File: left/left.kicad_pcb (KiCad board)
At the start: 2 copper layers, 117.6 x 97.9 mm, 53 parts, among them J1 USB_C_Receptacle_IN, J2 USB_C_Receptacle_OUT, SW1 SW_Push, SW2 SW_SPDT, U1 STM32G0B1CBTx, U2 SRV05-4, U3 XC6206P332MR, U4 SRV05-4

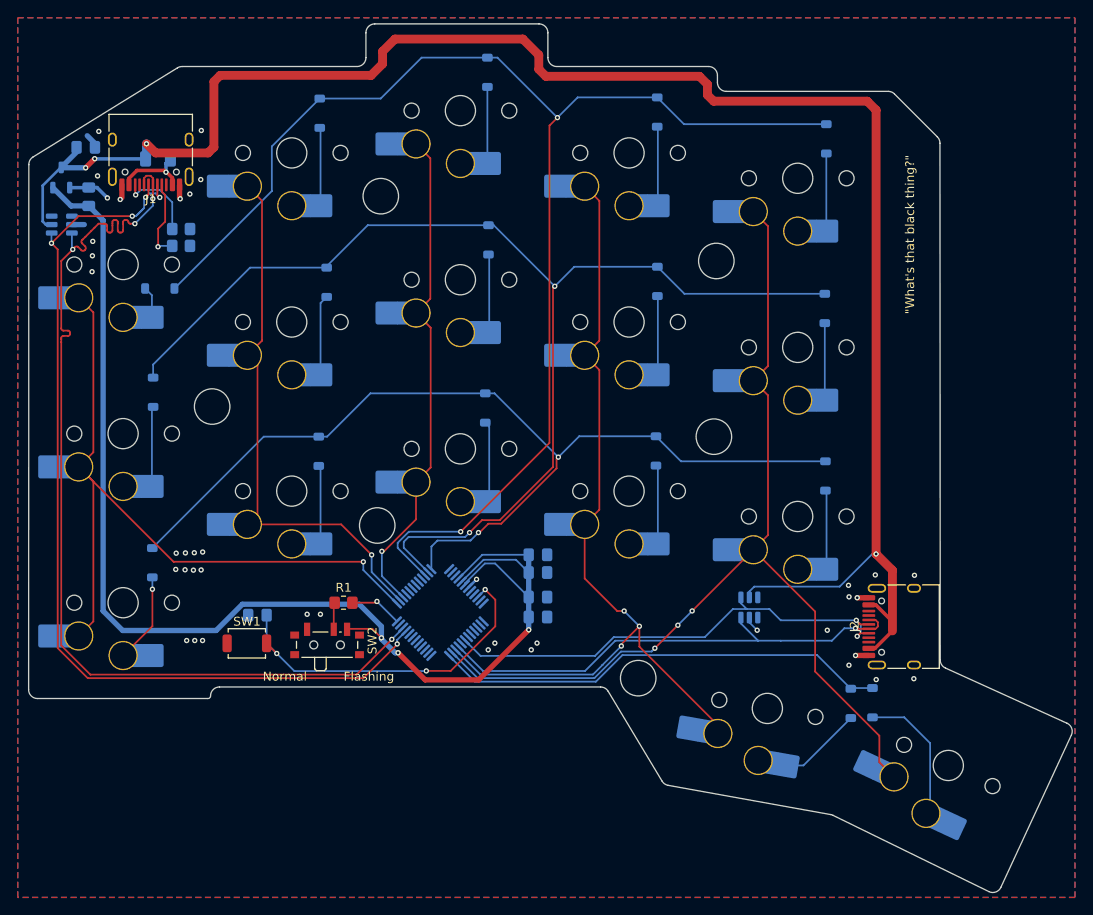
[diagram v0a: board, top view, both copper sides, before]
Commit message: needed to move the usbs on left side
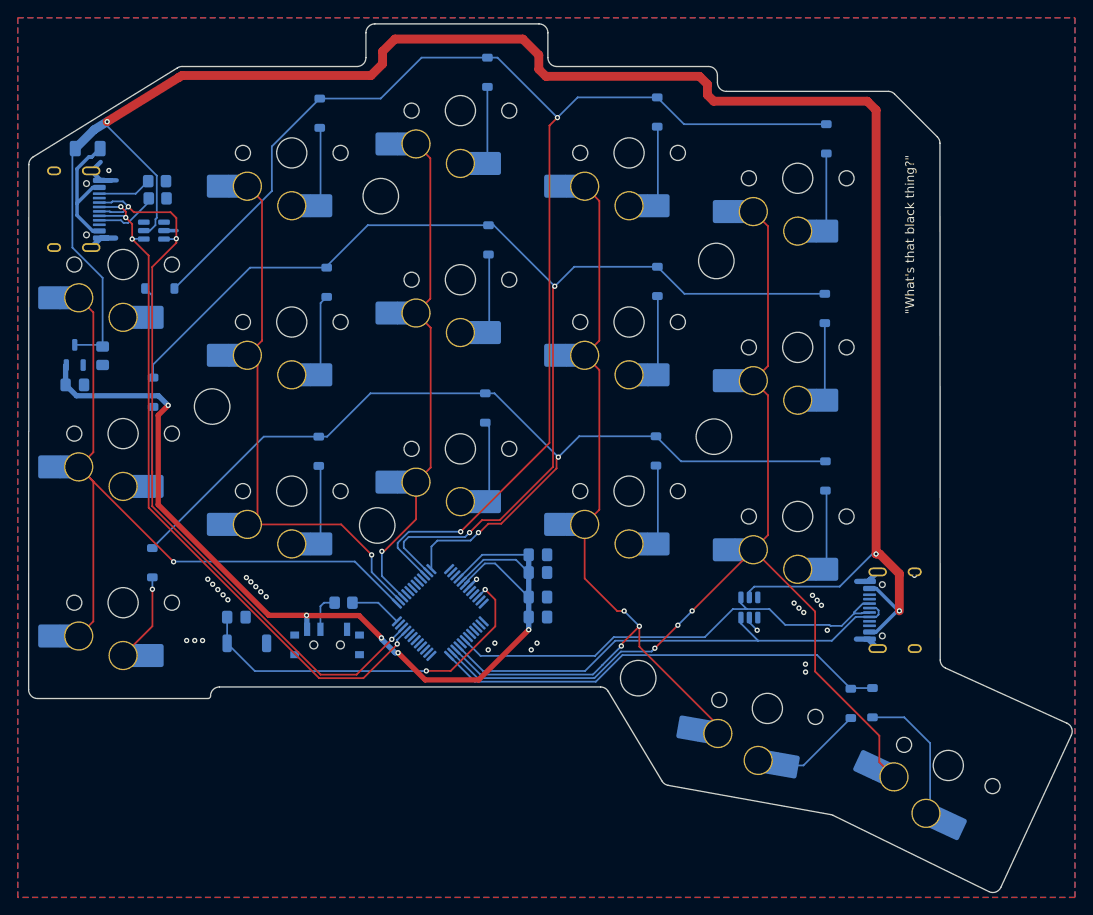
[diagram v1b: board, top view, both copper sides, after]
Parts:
- J1, J2, R1, SW1, SW2: moved to B.Cu
- moved C6 23.6 mm to (54.9, 83.4), turned to -90 degrees
- moved C7 21.3 mm to (51.7, 86.7), turned to 0 degrees
- moved U3 20.0 mm to (51.7, 83.3)
- moved J1 12.0 mm to (50.4, 66.9), turned to 90 degrees
- moved U4 10.4 mm to (60.6, 69.3)
- moved F1 8.00 mm to (53.2, 60.0)
- moved R2 6.03 mm to (61.0, 63.7)
- moved R3 5.97 mm to (61.1, 65.7)
- moved C5 2.38 mm to (69.9, 112.8), turned to 0 degrees
- moved J2 1.84 mm to (145.3, 112.0), turned to -90 degrees
- turned SW1 to 0 degrees
- turned SW2 to 180 degrees
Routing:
- net +3.3V: track 148.8 -> 116.8 mm, vias 3 -> 5
- net D-: track 109.7 -> 80.7 mm, vias 5 -> 4
- net D+: track 113.0 -> 85.8 mm, vias 4 -> 3
- net +5V: track 205.4 -> 226.2 mm, vias 4 -> 3
- net VBUS: track 8.91 -> 16.1 mm, vias 1 -> 0
- net Net-(J1-CC2): track 9.56 -> 5.66 mm, vias 1 -> 0
- net GND: track 17.4 -> 20.1 mm, vias 40 -> 30
- net nRST: track 40.0 -> 42.5 mm, vias 3 -> 2
- net Net-(J1-CC1): track 9.11 -> 6.65 mm, vias 1 -> 0
- net Net-(SW2-B): track 3.04 -> 4.36 mm
- net RX: track 54.6 -> 53.8 mm, vias 2 -> 0
- net COL4: track 83.6 -> 83.1 mm
- net TX: track 55.6 -> 56.1 mm, vias 1 -> 0
- net BOOT0: track 6.00 -> 5.88 mm, vias 1 -> 0

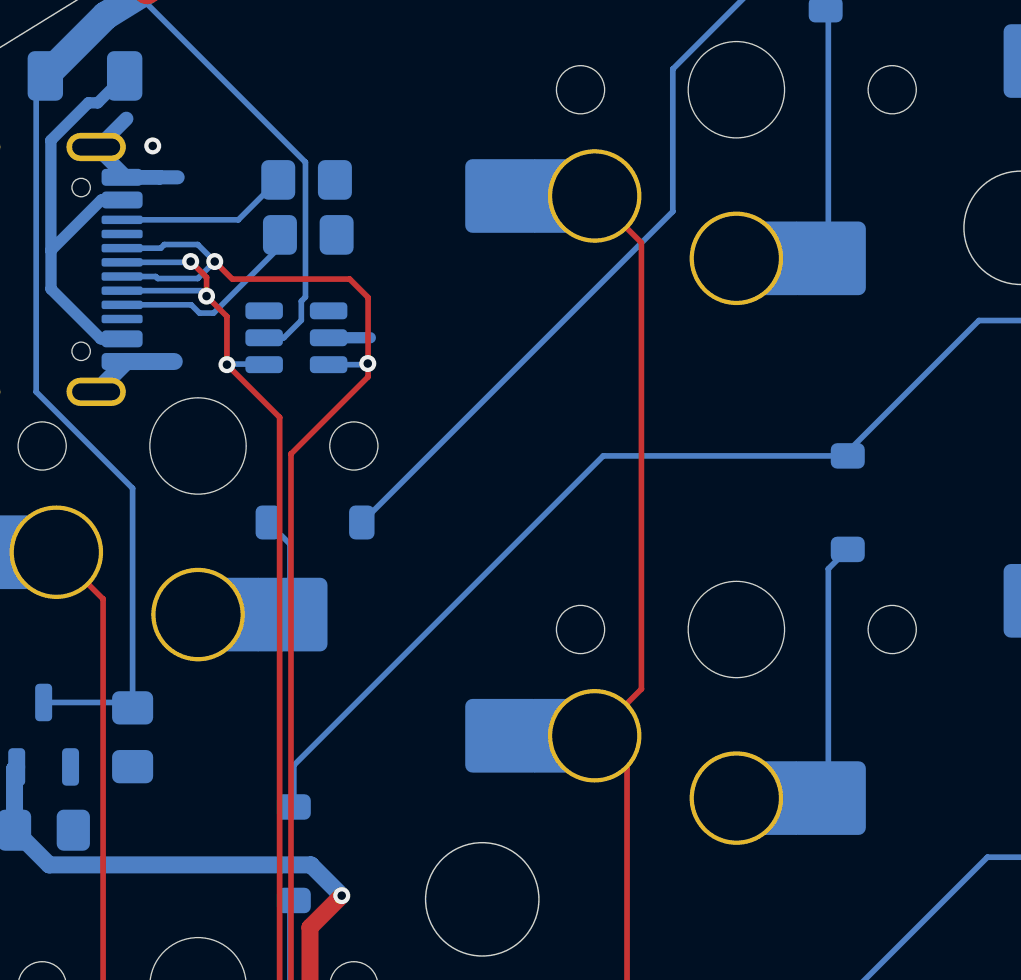
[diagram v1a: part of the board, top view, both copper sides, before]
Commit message: added vias to left to connect the zones a bit better
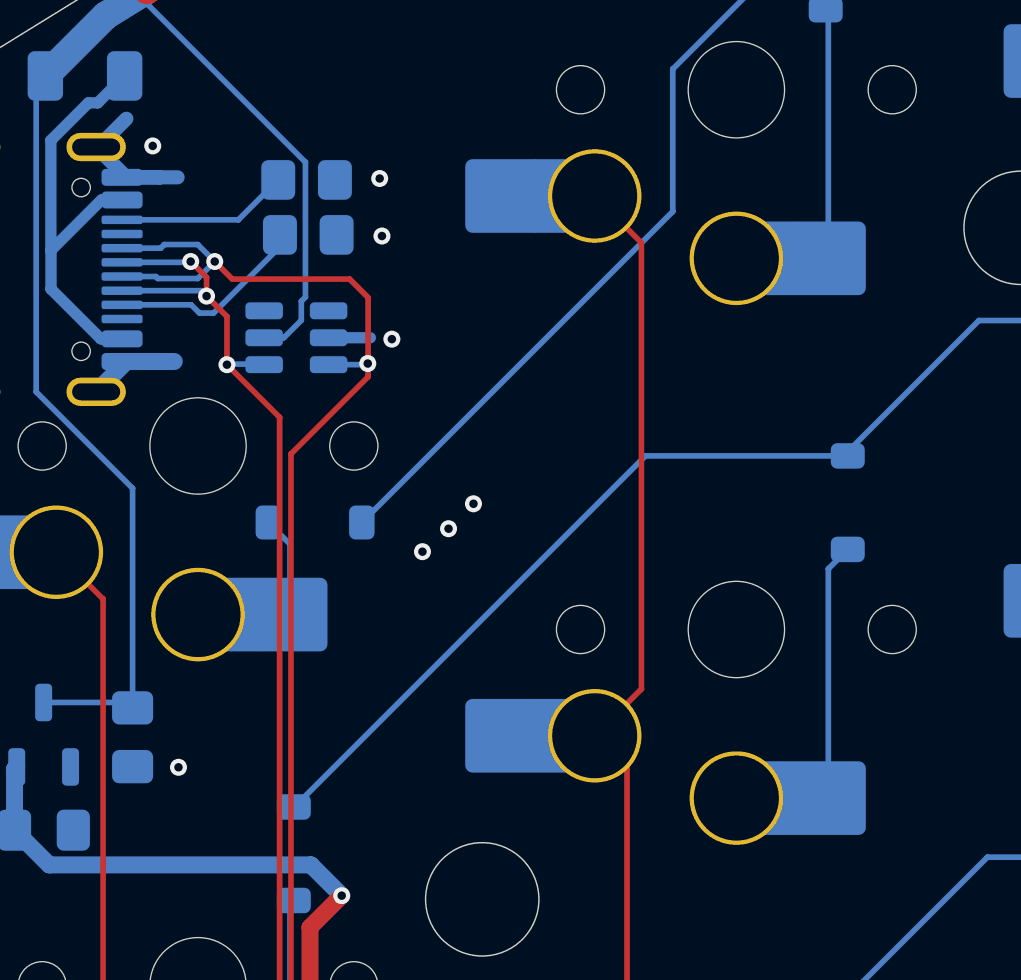
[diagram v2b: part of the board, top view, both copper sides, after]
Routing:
- net ROW1: track 134.1 -> 133.2 mm
- net GND: vias 30 -> 37
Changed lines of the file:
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@@
 	)
 	(via
+		(at 65.09 76.83)
+		(size 0.6)
+		(drill 0.3)
+		(layers "F.Cu" "B.Cu")
+		(free yes)
+		(net "GND")
+	)
+	(via
 		(at 132.76 111.24)
 		(size 0.6)
@@
 	)
 	(via
+		(at 64.01 69.33)
+		(size 0.6)
+		(drill 0.3)
+		(layers "F.Cu" "B.Cu")
+		(free yes)
+		(net "GND")
+	)
+	(via
 		(at 136.5 114.3)
 		(size 0.6)
@@
 	)
 	(via
+		(at 66.01 76.02)
+		(size 0.6)
+		(drill 0.3)
+		(layers "F.Cu" "B.Cu")
+		(free yes)
+		(net "GND")
+	)
+	(via
 		(at 133.85 112.3)
 		(size 0.6)
@@
 	)
 	(via
+		(at 66.89 75.14)
+		(size 0.6)
+		(drill 0.3)
+		(layers "F.Cu" "B.Cu")
+		(free yes)
+		(net "GND")
+	)
+	(via
 		(at 135.84 111.49)
 		(size 0.6)
@@
 	)
 	(via
+		(at 63.66 65.69)
+		(size 0.6)
+		(drill 0.3)
+		(layers "F.Cu" "B.Cu")
+		(free yes)
+		(net "GND")
+	)
+	(via
 		(at 146.32 108.11)
 		(size 0.6)
@@
 	)
 	(via
+		(at 56.48 84.44)
+		(size 0.6)
+		(drill 0.3)
+		(layers "F.Cu" "B.Cu")
+		(free yes)
+		(net "GND")
+	)
+	(via
 		(at 128.6 114.3)
 		(size 0.6)
@@
 	)
 	(via
+		(at 63.58 63.66)
+		(size 0.6)
+		(drill 0.3)
+		(layers "F.Cu" "B.Cu")
+		(free yes)
+		(net "GND")
+	)
+	(via
 		(at 65.24 115.46)
 		(size 0.6)
@@
 	)
 	(segment
-		(start 71.470054 73.45)
+		(start 72.96 73.45)
 		(end 80.1 73.45)
 		(width 0.2)
@@
 	)
 	(segment
+		(start 60.55 85.84)
+		(end 60.57 85.84)
+		(width 0.2)
+		(layer "B.Cu")
+		(net "ROW1")
+	)
+	(segment
 		(start 96.2 103.3)
 		(end 95.7 103.8)
@@
 	)
 	(segment
-		(start 60.55 84.370054)
-		(end 71.470054 73.45)
-		(width 0.2)
-		(layer "B.Cu")
-		(net "ROW1")
-	)
-	(segment
 		(start 95.7 103.8)
 		(end 89.325686 103.8)
@@
 	)
 	(segment
-		(start 89.325686 103.8)
-		(end 88.787843 104.337843)
+		(start 60.57 85.84)
+		(end 72.96 73.45)
 		(width 0.2)
 		(layer "B.Cu")
@@
 	)
 	(segment
-		(start 60.55 85.84)
-		(end 60.55 84.370054)
+		(start 89.325686 103.8)
+		(end 88.787843 104.337843)
 		(width 0.2)
 		(layer "B.Cu")
